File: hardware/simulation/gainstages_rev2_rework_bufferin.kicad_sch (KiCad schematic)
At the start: 32 parts, among them U1 ${SIM.PARAMS}, U2 ${SIM.PARAMS}, U3 ${SIM.PARAMS}

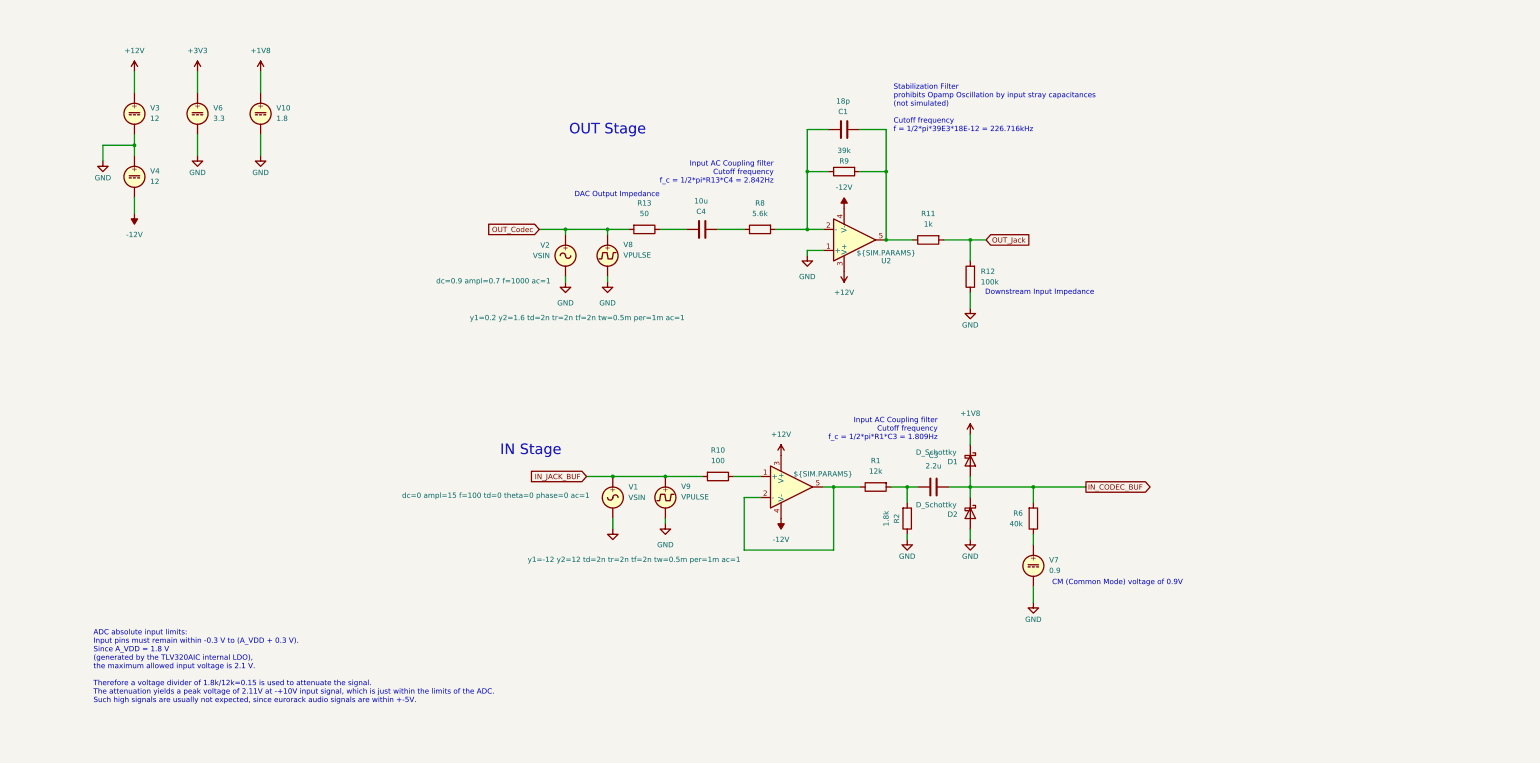
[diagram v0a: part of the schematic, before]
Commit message: hw: simulation updates
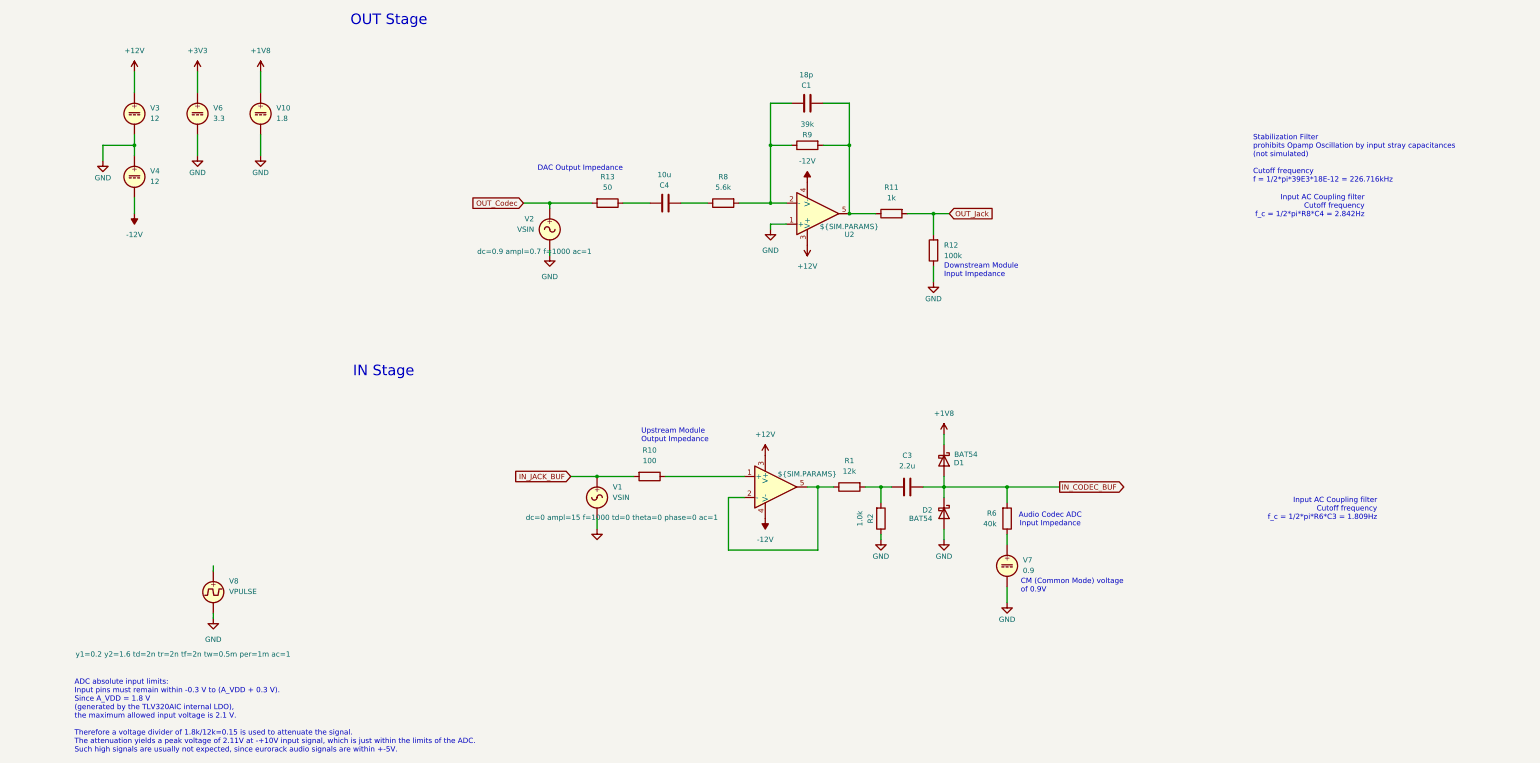
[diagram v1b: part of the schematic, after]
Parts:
- removed V9: VPULSE, symbol Simulation_SPICE:VPULSE
- D1, D2: value D_Schottky -> BAT54
- R2: value 1.8k -> 1.0k
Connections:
- net OUT_Codec: no longer V8.1
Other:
- note added: "Audio Codec ADC Input Impedance"
- note added: "Downstream Module Input Impedance"
- note added: "Input AC Coupling filter Cutoff frequency f_c = 1/2*pi*R6*C3 = 1.809Hz"
- note added: "Input AC Coupling filter Cutoff frequency f_c = 1/2*pi*R8*C4 = 2.842Hz"
- note added: "Upstream Module Output Impedance"
- note removed: "Downstream Input Impedance"
- note removed: "Input AC Coupling filter Cutoff frequency f_c = 1/2*pi*R1*C3 = 1.809Hz"
- note removed: "Input AC Coupling filter Cutoff frequency f_c = 1/2*pi*R13*C4 = 2.842Hz"
- moved on the sheet: C1, C3, C4, D1, D2, R1, R10, R11, R12, R13, R2, R6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
